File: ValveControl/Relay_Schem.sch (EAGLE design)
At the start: 68 parts, among them Q1 LINEAR_REGULATOR, Q2 LINEAR_REGULATOR, Q3 LINEAR_REGULATOR, Q4 LINEAR_REGULATOR, Q5 LINEAR_REGULATOR

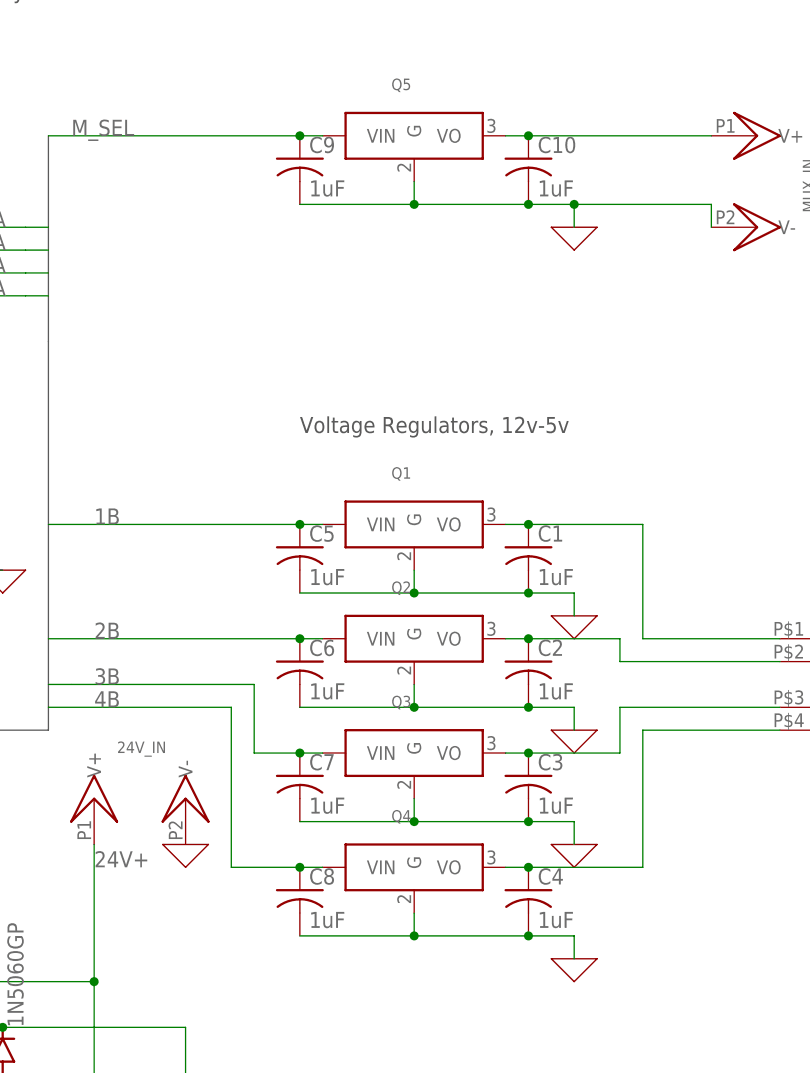
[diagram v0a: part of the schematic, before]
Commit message: Fix voltage regulators on board
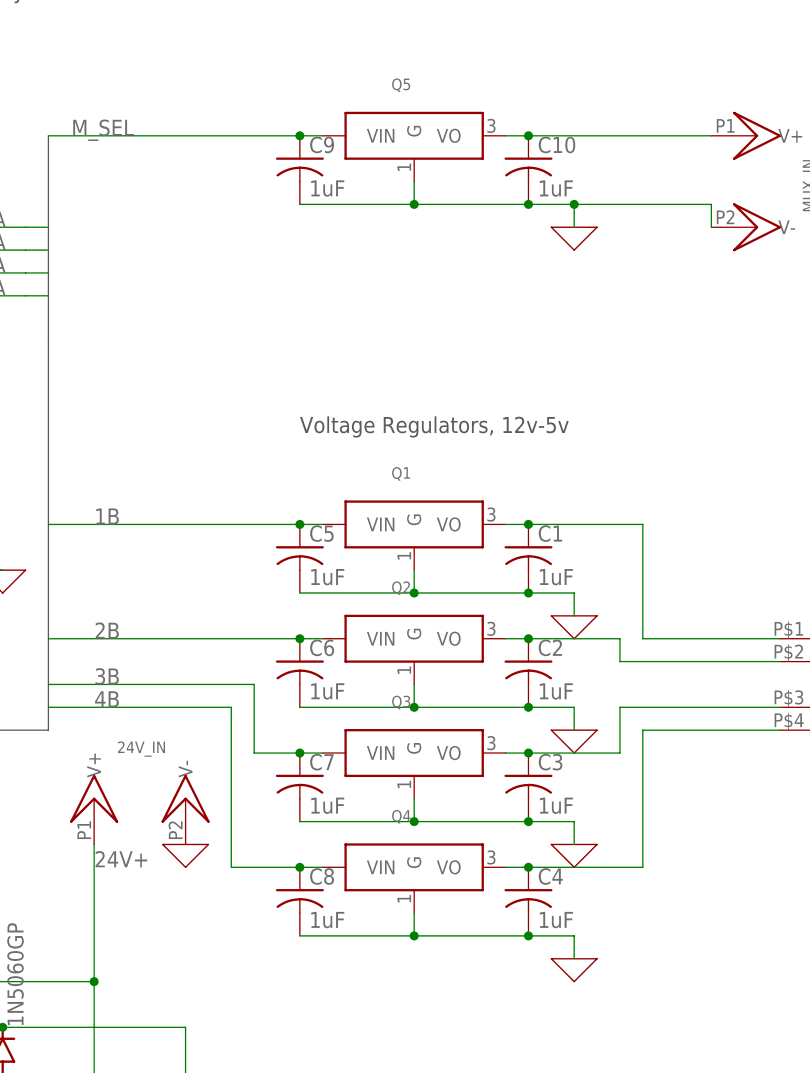
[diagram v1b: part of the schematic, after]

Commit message: More fixes/tweaks
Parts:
- 24V_IN: value COAX_POW -> COAX_POW_2.1MM; device LPRD_RELAY:COAX_POW -> LPRD_RELAY:COAX_POW_2.1MM
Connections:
- net 1B: now also Q1.VO; no longer Q1.VIN
- net 2B: now also Q2.VO; no longer Q2.VIN
- net 3B: now also Q3.VO; no longer Q3.VIN
- net 4B: now also Q4.VO; no longer Q4.VIN
- net M_SEL: now also Q5.VO; no longer Q5.VIN
- net N$1: now also Q1.VIN; no longer Q1.VO
- net N$12: now also Q4.VIN; no longer Q4.VO
- net N$2: now also Q2.VIN; no longer Q2.VO
- net N$24: now also Q5.VIN; no longer Q5.VO
- net N$4: now also Q3.VIN; no longer Q3.VO
- net N$6: no longer U$2.5V
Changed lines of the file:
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@@
 <part name="S3" library="LPRD_RELAY" deviceset="SSR_CPC1218Y" device=""/>
 <part name="S4" library="LPRD_RELAY" deviceset="SSR_CPC1218Y" device=""/>
-<part name="24V_IN" library="LPRD_RELAY" deviceset="COAX_POW" device=""/>
+<part name="24V_IN" library="LPRD_RELAY" deviceset="COAX_POW_2.1MM" device=""/>
 <part name="D1" library="diode" library_urn="urn:adsk.eagle:library:210" deviceset="1N5060GP" device="" package3d_urn="urn:adsk.eagle:package:43369/2"/>
 <part name="D2" library="diode" library_urn="urn:adsk.eagle:library:210" deviceset="1N5060GP" device="" package3d_urn="urn:adsk.eagle:package:43369/2"/>
@@
 </instance>
 <instance part="X_14" gate="G$1" x="154.94" y="142.24" smashed="yes"/>
-<instance part="Q1" gate="G$1" x="137.16" y="109.22" smashed="yes">
-<attribute name="NAME" x="134.62" y="114.3" size="1.27" layer="95"/>
-</instance>
-<instance part="Q2" gate="G$1" x="137.16" y="96.52" smashed="yes">
-<attribute name="NAME" x="134.62" y="101.6" size="1.27" layer="95"/>
-</instance>
-<instance part="Q3" gate="G$1" x="137.16" y="83.82" smashed="yes">
-<attribute name="NAME" x="134.62" y="88.9" size="1.27" layer="95"/>
-</instance>
-<instance part="Q4" gate="G$1" x="137.16" y="71.12" smashed="yes">
-<attribute name="NAME" x="134.62" y="76.2" size="1.27" layer="95"/>
-</instance>
-<instance part="Q5" gate="G$1" x="137.16" y="152.4" smashed="yes">
-<attribute name="NAME" x="134.62" y="157.48" size="1.27" layer="95"/>
+<instance part="Q1" gate="G$1" x="137.16" y="109.22" smashed="yes" rot="MR0">
+<attribute name="NAME" x="139.7" y="114.3" size="1.27" layer="95" rot="MR0"/>
+</instance>
+<instance part="Q2" gate="G$1" x="137.16" y="96.52" smashed="yes" rot="MR0">
+<attribute name="NAME" x="139.7" y="101.6" size="1.27" layer="95" rot="MR0"/>
+</instance>
+<instance part="Q3" gate="G$1" x="137.16" y="83.82" smashed="yes" rot="MR0">
+<attribute name="NAME" x="139.7" y="88.9" size="1.27" layer="95" rot="MR0"/>
+</instance>
+<instance part="Q4" gate="G$1" x="137.16" y="71.12" smashed="yes" rot="MR0">
+<attribute name="NAME" x="139.7" y="76.2" size="1.27" layer="95" rot="MR0"/>
+</instance>
+<instance part="Q5" gate="G$1" x="137.16" y="152.4" smashed="yes" rot="MR0">
+<attribute name="NAME" x="139.7" y="157.48" size="1.27" layer="95" rot="MR0"/>
 </instance>
 <instance part="CTRL_IN" gate="G$1" x="187.96" y="91.44" smashed="yes">
@@
 <wire x1="96.52" y1="109.22" x2="124.46" y2="109.22" width="0.1524" layer="91"/>
 <pinref part="C5" gate="G$1" pin="1"/>
+<label x="101.6" y="109.22" size="1.778" layer="95"/>
+<pinref part="Q1" gate="G$1" pin="VO"/>
 <wire x1="124.46" y1="109.22" x2="127" y2="109.22" width="0.1524" layer="91"/>
 <junction x="124.46" y="109.22"/>
-<label x="101.6" y="109.22" size="1.778" layer="95"/>
-<pinref part="Q1" gate="G$1" pin="VIN"/>
 </segment>
 <segment>
@@
 <wire x1="96.52" y1="96.52" x2="124.46" y2="96.52" width="0.1524" layer="91"/>
 <pinref part="C6" gate="G$1" pin="1"/>
+<label x="101.6" y="96.52" size="1.778" layer="95"/>
+<pinref part="Q2" gate="G$1" pin="VO"/>
 <wire x1="124.46" y1="96.52" x2="127" y2="96.52" width="0.1524" layer="91"/>
 <junction x="124.46" y="96.52"/>
-<label x="101.6" y="96.52" size="1.778" layer="95"/>
-<pinref part="Q2" gate="G$1" pin="VIN"/>
 </segment>
 <segment>
@@
 </segment>
 <segment>
-<wire x1="127" y1="71.12" x2="124.46" y2="71.12" width="0.1524" layer="91"/>
 <wire x1="124.46" y1="71.12" x2="116.84" y2="71.12" width="0.1524" layer="91"/>
 <wire x1="116.84" y1="71.12" x2="116.84" y2="88.9" width="0.1524" layer="91"/>
 <wire x1="96.52" y1="88.9" x2="116.84" y2="88.9" width="0.1524" layer="91"/>
 <pinref part="C8" gate="G$1" pin="1"/>
+<label x="101.6" y="88.9" size="1.778" layer="95"/>
+<pinref part="Q4" gate="G$1" pin="VO"/>
+<wire x1="127" y1="71.12" x2="124.46" y2="71.12" width="0.1524" layer="91"/>
 <junction x="124.46" y="71.12"/>
-<label x="101.6" y="88.9" size="1.778" layer="95"/>
-<pinref part="Q4" gate="G$1" pin="VIN"/>
 </segment>
 <segment>
@@
 </segment>
 <segment>
-<wire x1="127" y1="83.82" x2="124.46" y2="83.82" width="0.1524" layer="91"/>
 <wire x1="124.46" y1="83.82" x2="119.38" y2="83.82" width="0.1524" layer="91"/>
 <wire x1="119.38" y1="83.82" x2="119.38" y2="91.44" width="0.1524" layer="91"/>
-<wire x1="119.38" y1="91.44" x2="101.6" y2="91.44" width="0.1524" layer="91"/>
-<wire x1="101.6" y1="91.44" x2="99.06" y2="91.44" width="0.1524" layer="91"/>
+<wire x1="119.38" y1="91.44" x2="96.52" y2="91.44" width="0.1524" layer="91"/>
 <pinref part="C7" gate="G$1" pin="1"/>
+<label x="101.6" y="91.44" size="1.778" layer="95"/>
+<pinref part="Q3" gate="G$1" pin="VO"/>
+<wire x1="124.46" y1="83.82" x2="127" y2="83.82" width="0.1524" layer="91"/>
 <junction x="124.46" y="83.82"/>
-<label x="101.6" y="91.44" size="1.778" layer="95"/>
-<wire x1="99.06" y1="91.44" x2="96.52" y2="91.44" width="0.1524" layer="91"/>
-<pinref part="Q3" gate="G$1" pin="VIN"/>
 </segment>
 <segment>
@@
 <pinref part="C1" gate="G$1" pin="1"/>
 <wire x1="162.56" y1="109.22" x2="149.86" y2="109.22" width="0.1524" layer="91"/>
+<pinref part="CTRL_IN" gate="G$1" pin="P1"/>
+<pinref part="Q1" gate="G$1" pin="VIN"/>
 <wire x1="147.32" y1="109.22" x2="149.86" y2="109.22" width="0.1524" layer="91"/>
 <junction x="149.86" y="109.22"/>
-<pinref part="Q1" gate="G$1" pin="VO"/>
-<pinref part="CTRL_IN" gate="G$1" pin="P1"/>
 </segment>
 </net>
@@
 <segment>
 <pinref part="C2" gate="G$1" pin="1"/>
-<wire x1="147.32" y1="96.52" x2="149.86" y2="96.52" width="0.1524" layer="91"/>
 <wire x1="149.86" y1="96.52" x2="160.02" y2="96.52" width="0.1524" layer="91"/>
-<junction x="149.86" y="96.52"/>
 <wire x1="160.02" y1="96.52" x2="160.02" y2="93.98" width="0.1524" layer="91"/>
 <wire x1="160.02" y1="93.98" x2="177.8" y2="93.98" width="0.1524" layer="91"/>
-<pinref part="Q2" gate="G$1" pin="VO"/>
 <pinref part="CTRL_IN" gate="G$1" pin="P2"/>
+<pinref part="Q2" gate="G$1" pin="VIN"/>
+<wire x1="147.32" y1="96.52" x2="149.86" y2="96.52" width="0.1524" layer="91"/>
+<junction x="149.86" y="96.52"/>
 </segment>
 </net>
@@
 <wire x1="160.02" y1="83.82" x2="149.86" y2="83.82" width="0.1524" layer="91"/>
 <pinref part="C3" gate="G$1" pin="1"/>
-<wire x1="149.86" y1="83.82" x2="147.32" y2="83.82" width="0.1524" layer="91"/>
+<pinref part="CTRL_IN" gate="G$1" pin="P3"/>
+<pinref part="Q3" gate="G$1" pin="VIN"/>
+<wire x1="147.32" y1="83.82" x2="149.86" y2="83.82" width="0.1524" layer="91"/>
 <junction x="149.86" y="83.82"/>
-<pinref part="Q3" gate="G$1" pin="VO"/>
-<pinref part="CTRL_IN" gate="G$1" pin="P3"/>
 </segment>
 </net>
@@
 <wire x1="162.56" y1="71.12" x2="149.86" y2="71.12" width="0.1524" layer="91"/>
 <pinref part="C4" gate="G$1" pin="1"/>
-<wire x1="149.86" y1="71.12" x2="147.32" y2="71.12" width="0.1524" layer="91"/>
+<pinref part="CTRL_IN" gate="G$1" pin="P4"/>
+<pinref part="Q4" gate="G$1" pin="VIN"/>
+<wire x1="147.32" y1="71.12" x2="149.86" y2="71.12" width="0.1524" layer="91"/>
 <junction x="149.86" y="71.12"/>
-<pinref part="Q4" gate="G$1" pin="VO"/>
-<pinref part="CTRL_IN" gate="G$1" pin="P4"/>
 </segment>
 </net>
@@
 </segment>
 <segment>
-<wire x1="127" y1="152.4" x2="124.46" y2="152.4" width="0.1524" layer="91"/>
 <label x="99.06" y="152.4" size="1.778" layer="95"/>
 <pinref part="C9" gate="G$1" pin="1"/>
 <wire x1="124.46" y1="152.4" x2="96.52" y2="152.4" width="0.1524" layer="91"/>
+<pinref part="Q5" gate="G$1" pin="VO"/>
+<wire x1="124.46" y1="152.4" x2="127" y2="152.4" width="0.1524" layer="91"/>
 <junction x="124.46" y="152.4"/>
-<pinref part="Q5" gate="G$1" pin="VIN"/>
 </segment>
 </net>
@@
 <net name="N$6" class="0">
 <segment>
+<pinref part="MUX" gate="G$1" pin="VCC"/>
+<wire x1="-33.02" y1="40.64" x2="-33.02" y2="96.52" width="0.1524" layer="91"/>
+<pinref part="U$2" gate="G$1" pin="GND@5"/>
 <pinref part="U$2" gate="G$1" pin="GND@4"/>
-<pinref part="U$2" gate="G$1" pin="GND@5"/>
 <wire x1="78.74" y1="153.67" x2="81.28" y2="153.67" width="0.1524" layer="91"/>
 <wire x1="78.74" y1="153.67" x2="73.66" y2="153.67" width="0.1524" layer="91"/>
-<wire x1="73.66" y1="153.67" x2="73.66" y2="139.7" width="0.1524" layer="91"/>
+<wire x1="73.66" y1="153.67" x2="73.66" y2="114.3" width="0.1524" layer="91"/>
 <junction x="78.74" y="153.67"/>
-<wire x1="73.66" y1="139.7" x2="73.66" y2="116.84" width="0.1524" layer="91"/>
-<wire x1="73.66" y1="116.84" x2="22.86" y2="116.84" width="0.1524" layer="91"/>
-<pinref part="MUX" gate="G$1" pin="VCC"/>
-<wire x1="-33.02" y1="40.64" x2="-33.02" y2="96.52" width="0.1524" layer="91"/>
-<wire x1="-33.02" y1="96.52" x2="22.86" y2="96.52" width="0.1524" layer="91"/>
-<pinref part="U$2" gate="G$1" pin="5V"/>
-<wire x1="22.86" y1="96.52" x2="22.86" y2="105.41" width="0.1524" layer="91"/>
-<wire x1="22.86" y1="116.84" x2="22.86" y2="105.41" width="0.1524" layer="91"/>
-<junction x="22.86" y="105.41"/>
+<wire x1="73.66" y1="114.3" x2="7.62" y2="114.3" width="0.1524" layer="91"/>
+<wire x1="7.62" y1="114.3" x2="7.62" y2="96.52" width="0.1524" layer="91"/>
+<wire x1="-33.02" y1="96.52" x2="7.62" y2="96.52" width="0.1524" layer="91"/>
 </segment>
 </net>
@@
 <segment>
 <pinref part="C10" gate="G$1" pin="1"/>
-<wire x1="149.86" y1="152.4" x2="147.32" y2="152.4" width="0.1524" layer="91"/>
 <wire x1="149.86" y1="152.4" x2="170.18" y2="152.4" width="0.1524" layer="91"/>
+<pinref part="MUX_IN" gate="G$1" pin="V+"/>
+<pinref part="Q5" gate="G$1" pin="VIN"/>
+<wire x1="147.32" y1="152.4" x2="149.86" y2="152.4" width="0.1524" layer="91"/>
 <junction x="149.86" y="152.4"/>
-<pinref part="Q5" gate="G$1" pin="VO"/>
-<pinref part="MUX_IN" gate="G$1" pin="V+"/>
-</segment>
-</net>
+</segment>
+</net>

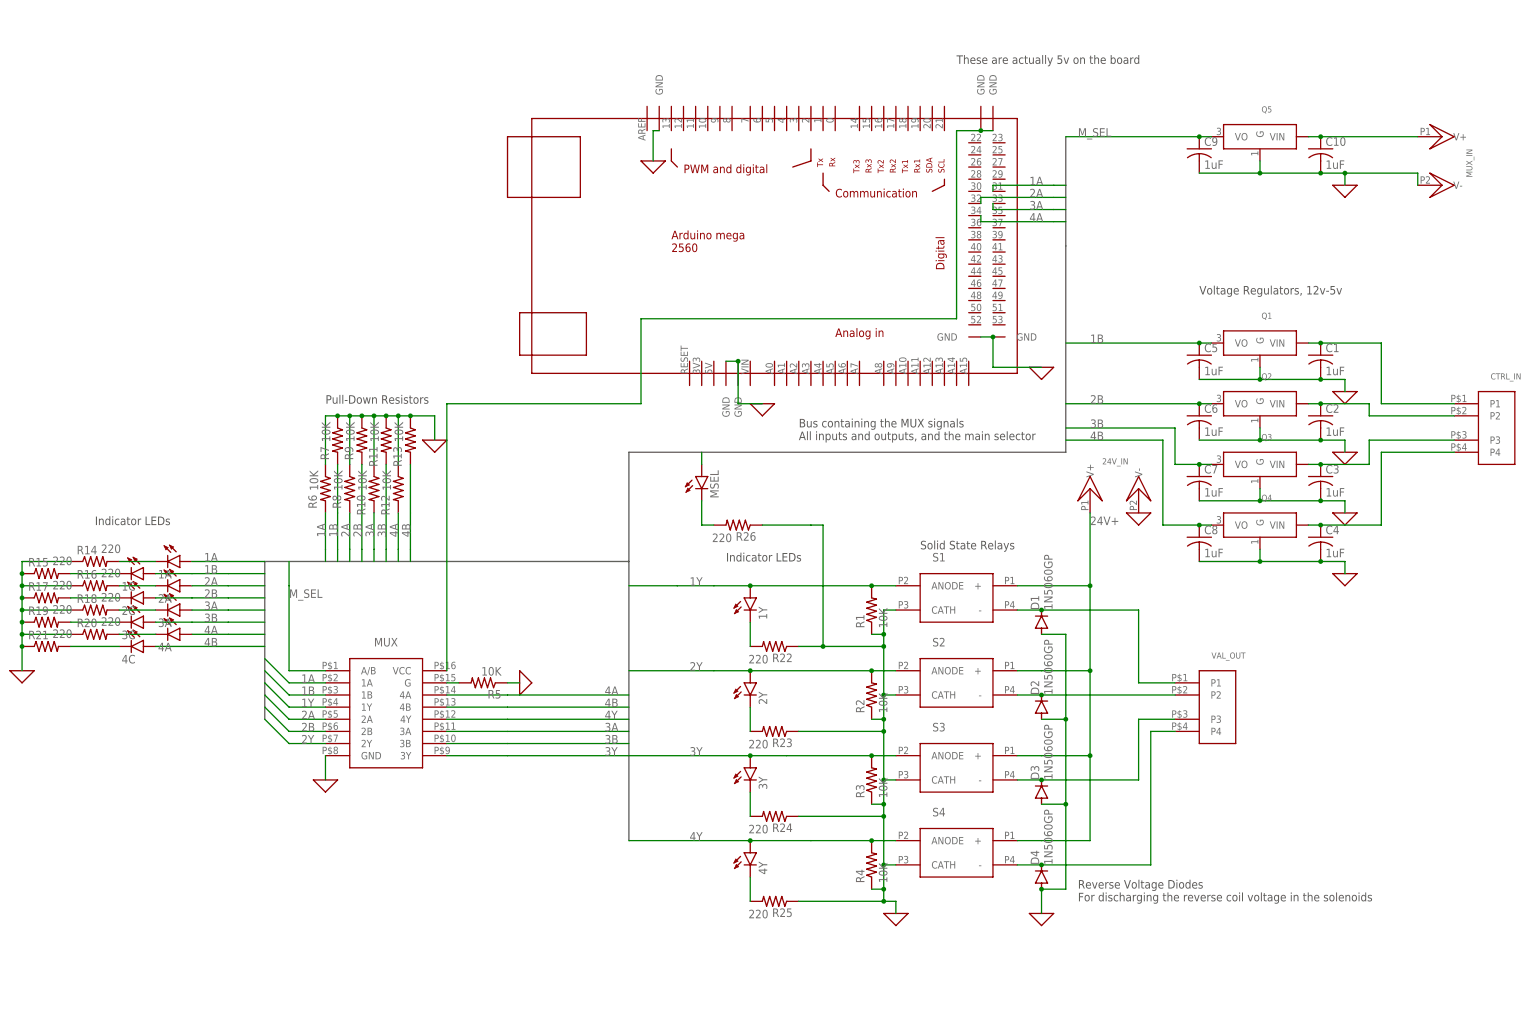
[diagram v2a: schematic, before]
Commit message: Update schematic for valve board
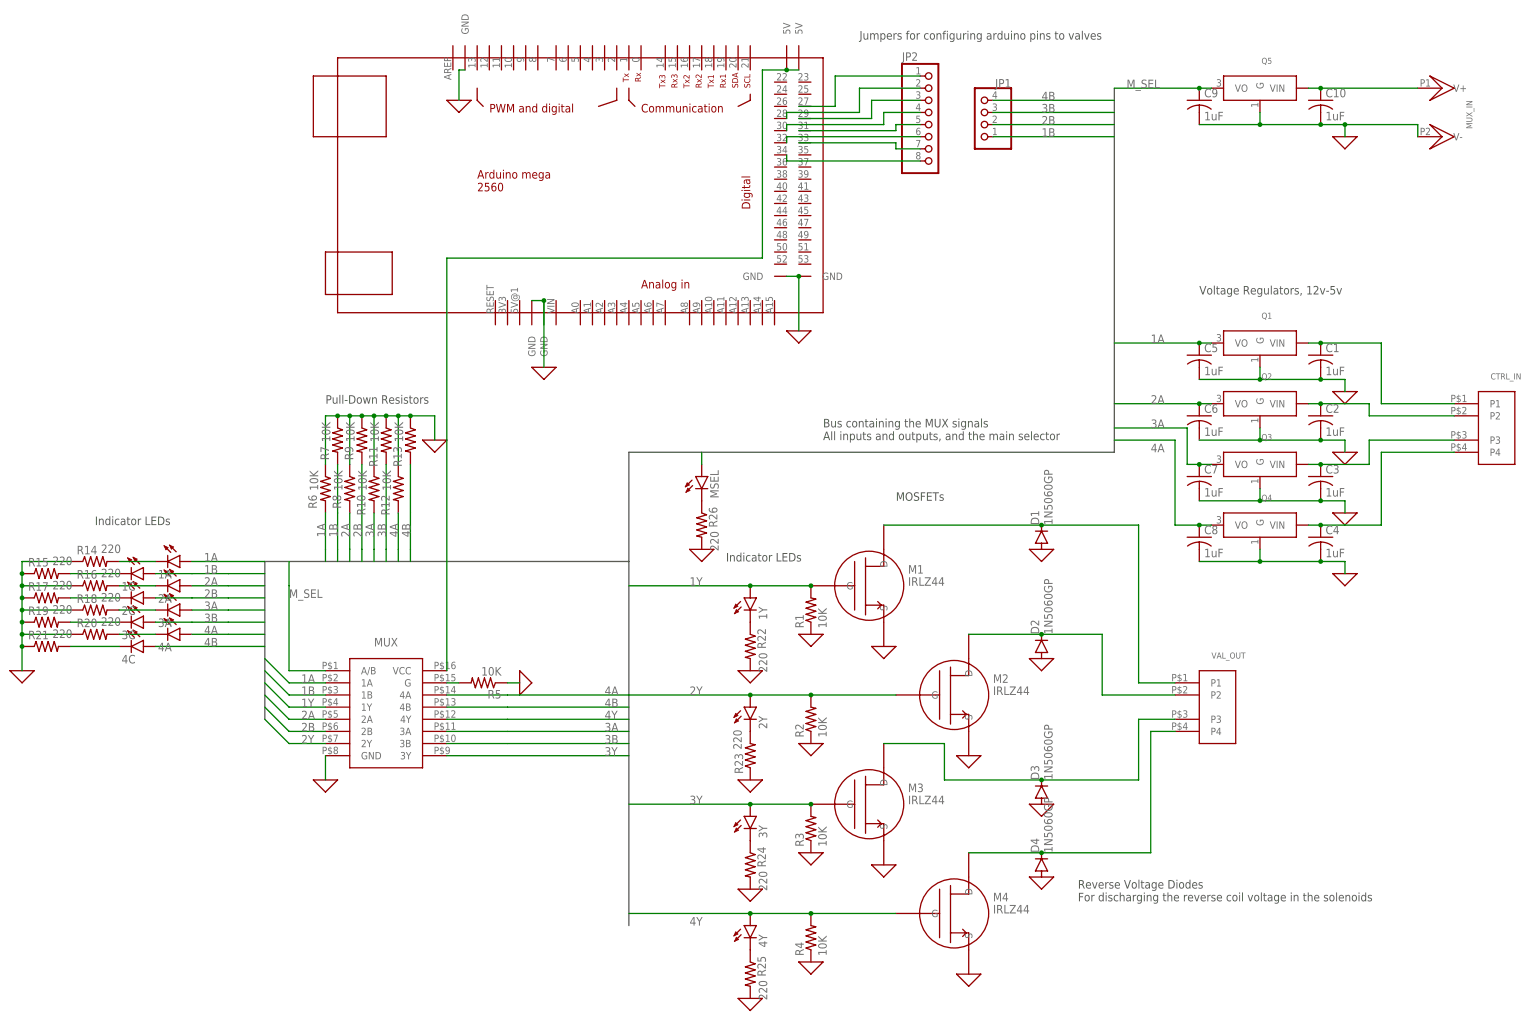
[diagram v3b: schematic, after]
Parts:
- removed 24V_IN: COAX_POW_2.1MM, LPRD_RELAY:COAX_POW_2.1MM
- removed S1, S2, S3, S4: SSR_CPC1218Y, LPRD_RELAY:SSR_CPC1218Y
- added JP1: (no value), pinhead:PINHD-1X4
- added JP2: (no value), pinhead:PINHD-1X8
- added M1, M2, M3, M4: IRLZ44, ngspice-simulation:FET_N
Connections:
- removed net 24V+: 24V_IN.V+, S1.+, S2.+, S3.+, S4.+
- new net N$25: JP2.1, U$2.27
- new net N$26: JP2.2, U$2.28
- new net N$27: JP2.3, U$2.29
- new net N$28: JP2.4, U$2.30
- new net N$29: JP2.5, U$2.31
- new net N$30: JP2.6, U$2.32
- new net N$31: JP2.7, U$2.33
- new net N$32: JP2.8, U$2.34
- net 0: now also M1.S, M2.S, M3.S, M4.S, R22.2, R24.2, R25.2, R26.2, U$2.GND@4, U$2.GND@5; no longer 24V_IN.V-, R22.1, R24.1, R25.1, R26.1, S1.CATH, S2.CATH, S3.CATH, S4.CATH, U$2.GND@6, U$2.GND@7
- net 1A: now also C5.1, Q1.VO; no longer U$2.31
- net 1B: now also JP1.1; no longer C5.1, Q1.VO
- net 1Y: now also M1.G; no longer S1.ANODE
- net 2A: now also C6.1, Q2.VO; no longer U$2.32
- net 2B: now also JP1.2; no longer C6.1, Q2.VO
- net 2Y: now also M2.G; no longer S2.ANODE
- net 3A: now also C7.1, Q3.VO; no longer U$2.33
- net 3B: now also JP1.3; no longer C7.1, Q3.VO
- net 3Y: now also M3.G; no longer S3.ANODE
- net 4A: now also C8.1, Q4.VO; no longer U$2.34
- net 4B: now also JP1.4; no longer C8.1, Q4.VO
- net 4Y: now also M4.G; no longer S4.ANODE
- net N$11: now also R22.1; no longer R22.2
- net N$22: now also R24.1; no longer R24.2
- net N$23: now also R25.1; no longer R25.2
- net N$3: now also M1.D; no longer S1.-
- net N$5: now also M2.D; no longer S2.-
- net N$6: now also U$2.5V@2, U$2.5V@3; no longer U$2.GND@4, U$2.GND@5
- net N$7: now also R26.1; no longer R26.2
- net N$8: now also M3.D; no longer S3.-
- net N$9: now also M4.D; no longer S4.-
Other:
- note added: "Jumpers for configuring arduino pins to valves"
- note added: "MOSFETs"
- note removed: "Solid State Relays"
- note removed: "These are actually 5v on the board"
- moved on the sheet: 2Y, 3Y, 4Y, C10, C9, D1, D2, D4, MUX_IN, Q5, R1, R2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
